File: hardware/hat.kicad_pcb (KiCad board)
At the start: 4 copper layers, 65 x 56.6 mm, 133 parts, among them J101 Raspberry_Pi_2_3, J102 Boot, J201 USB-C, P101 Debug, P201 Black, P301 CON-SENSOR2, P302 CON-SENSOR2, P303 CON-SENSOR2, P304 CON-SENSOR2, P305 CON-SENSOR2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

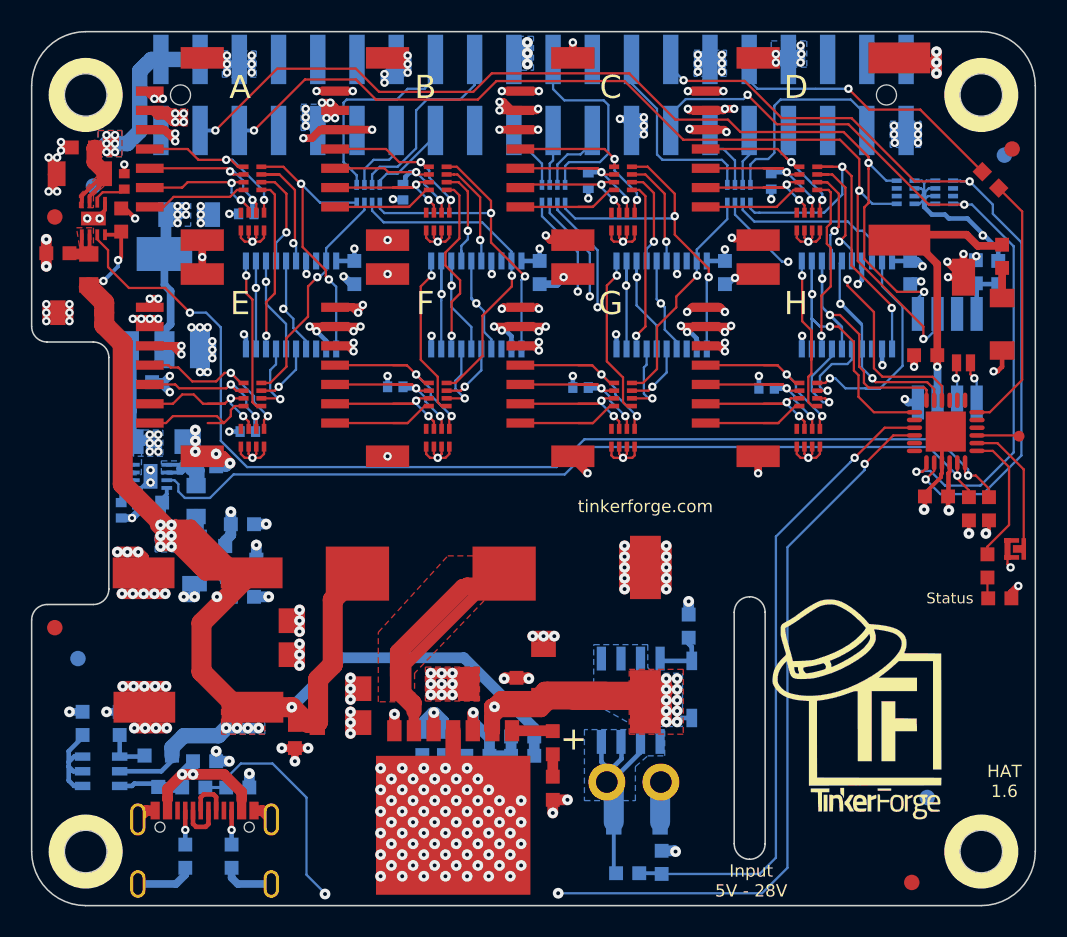
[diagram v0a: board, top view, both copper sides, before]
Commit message: add version 1.7
add step down filters
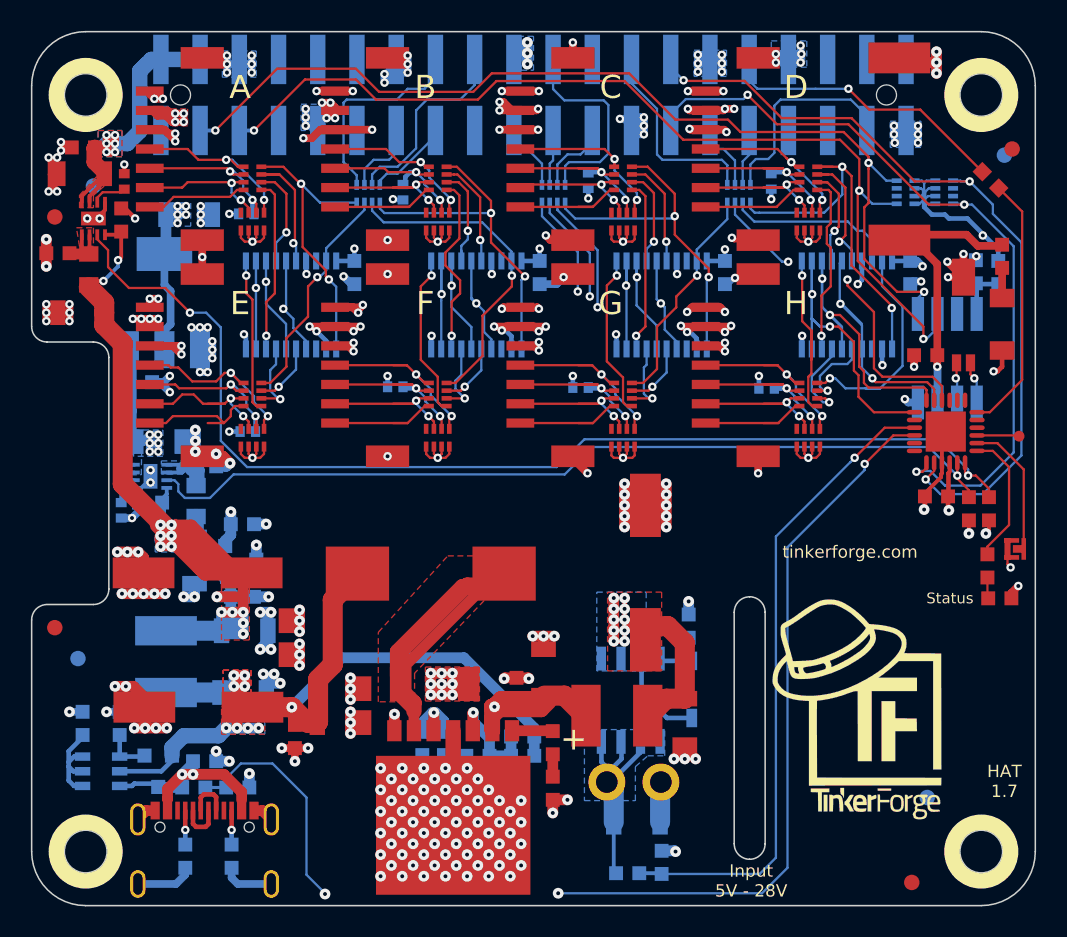
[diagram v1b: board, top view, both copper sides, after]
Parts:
- added C214: 10uF, C1206, F.Cu at (208.5, 70.1)
- added C215: 10uF, C1206, B.Cu at (180.0, 64.2)
- added C216: 10uF, C1206, B.Cu at (179.9, 68.2)
- added L202: 2.2uH 0530CDMCCDS-2R2MC, kicad-libraries:NRS5030, F.Cu at (204.1, 69.7)
- added L203: 2.2uH 0530CDMCCDS-2R2MC, kicad-libraries:NRS5030, B.Cu at (174.9, 66.2)
- moved C202 4.02 mm to (205.9, 60.4)
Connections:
- C202 pad 1: VIN2 -> VIN1
- C206 pad 1: +5V -> 5VF
- C208 pad 1: +5V -> 5VF
- C209 pad 1: +5V -> 5VF
- C210 pad 1: +5V -> 5VF
- C211 pad 1: +5V -> 5VF
- C212 pad 1: +5V -> 5VF
- C213 pad 1: +5V -> 5VF
- D202 pad 2: VIN2 -> VIN1
- L201 pad 2: +5V -> 5VF
- Q201 pad S: +5V -> 5VF
- Q202 pad S: VIN2 -> VIN1
- R209 pad 2: +5V -> 5VF
- U202 pad 5: +5V -> 5VF
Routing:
- net 5VF: track 0.00 -> 61.4 mm, vias 0 -> 9
- net +5V: track 115.9 -> 70.9 mm
- net VIN2: track 54.9 -> 22.8 mm, vias 12 -> 2
- net VIN1: track 0.00 -> 22.4 mm, vias 0 -> 10
- net GND: track 609.9 -> 620.6 mm, vias 290 -> 297
- added copper zone on B.Cu, net 5VF
- added copper zone on F.Cu, net 5VF
- added copper zone on B.Cu, net VIN1
- added copper zone on F.Cu, net VIN1
- removed copper zone on B.Cu, net VIN2
- removed copper zone on F.Cu, net VIN2
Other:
- board text added: "Copyright Tinkerforge GmbH 2021. This documentation describes Open Hardware and is licensed under the CERN OHL v. 1.1. You may redistribute and modify this documentation under the terms of the CERN OHL v.1.1. (http://ohwr.org/cernohl). This documentation is distributed WITHOUT ANY EXPRESS OR IMPLIED WARRANTY, INCLUDING OF MERCHANTABILITY, SATISFACTORY QUALITY AND FITNESS FOR A PARTICULAR PURPOSE.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"
- board text added: "HAT 1.7"
- board text removed: "Copyright Tinkerforge GmbH 2020. This documentation describes Open Hardware and is licensed under the CERN OHL v. 1.1. You may redistribute and modify this documentation under the terms of the CERN OHL v.1.1. (http://ohwr.org/cernohl). This documentation is distributed WITHOUT ANY EXPRESS OR IMPLIED WARRANTY, INCLUDING OF MERCHANTABILITY, SATISFACTORY QUALITY AND FITNESS FOR A PARTICULAR PURPOSE.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"
- board text removed: "HAT 1.6"

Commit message: switched to kicad 6
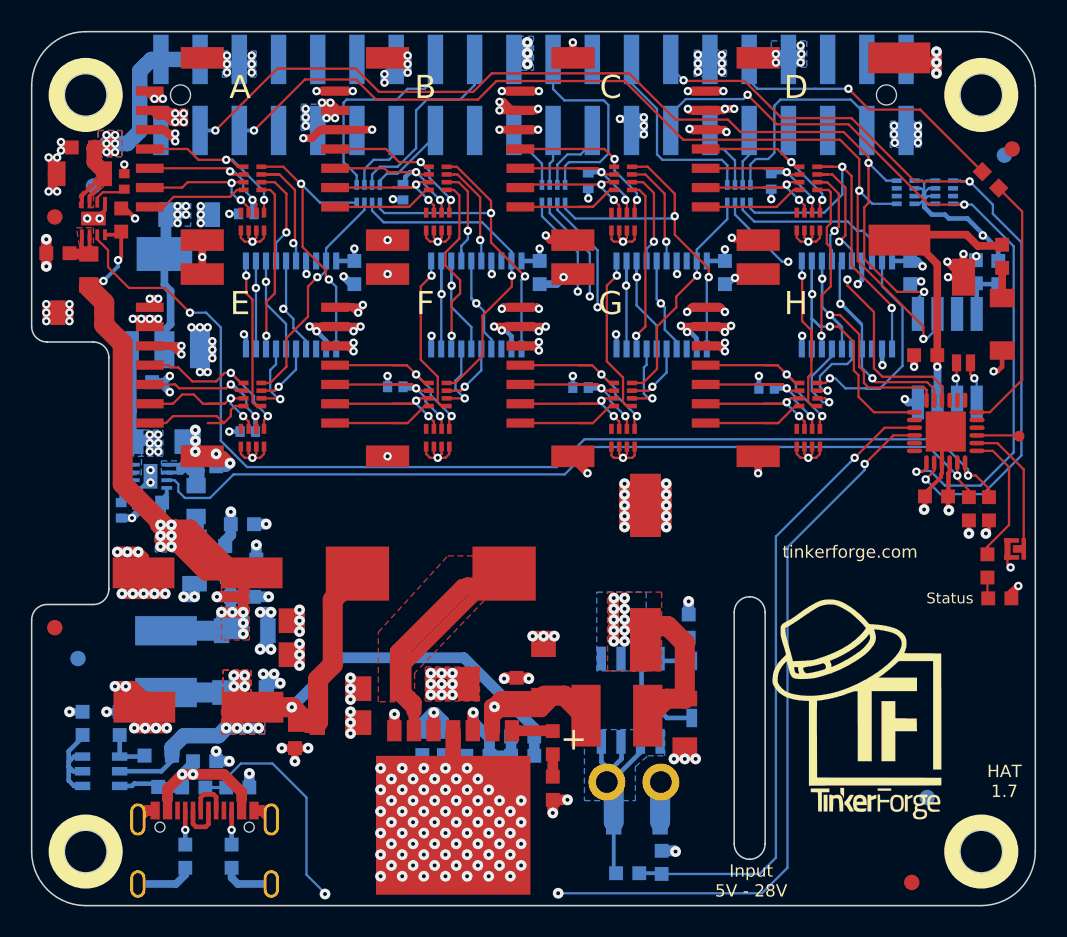
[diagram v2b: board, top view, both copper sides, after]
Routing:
- added copper zone on In2.Cu, net 3V3
- added copper zone on In2.Cu, net B-3V3
- added copper zone on In2.Cu, net B-5V
- added copper zone on In1.Cu, net GND
- removed copper zone on VCC, net 3V3
- removed copper zone on VCC, net B-3V3
- removed copper zone on VCC, net B-5V
- removed copper zone on GND, net GND
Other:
- net class Default removed

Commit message: Proto V1.8
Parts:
- removed C202: UWT1H221MNL1GS, kicad-libraries:ELKO_103
- removed C204, C208: 100nF, C0603F
- removed C205: 100pF, C0603F
- removed C206, C209, C212, C213, C215, C216: 10uF, C1206
- removed C207: 4.7nF, C0603F
- removed C210: 470µF/16V, kicad-libraries:ELKO_83
- removed C211: DNP, C0603F
- removed D201: PMEG6045, SOD-128
- removed Fiducial_Mark (x8): VAL**, kicad-libraries:Fiducial_Mark
- removed the G*** at (198.7, 54.0)
- removed L203: 2.2uH 0530CDMCCDS-2R2MC, kicad-libraries:NRS5030
- removed R201: 27k, R0603F
- removed R206: 20k, R0603F
- removed R209: 47k, R0603F
- removed R210: 8.2k, R0603F
- removed U201: BD906XX-C-HRP7, BD906XX-C-HRP7
- removed VAL: WEEE_7mm, kicad-libraries:WEEE_7mm
- removed VAL: CE_5mm, kicad-libraries:CE_5mm
- added C1: 47uF, kicad-libraries:C1210, F.Cu at (194.2, 67.9)
- added C2: 47uF, kicad-libraries:C1210, F.Cu at (189.8, 67.9)
- added C3: 10uF, kicad-libraries:C0805E, B.Cu at (178.6, 66.9)
- added C4: 10uF, kicad-libraries:C0805E, B.Cu at (176.7, 66.9)
- added C5: 100nF, kicad-libraries:C0603F, B.Cu at (175.1, 66.9)
- added C6: 10uF/50V, kicad-libraries:C1210, F.Cu at (189.8, 59.1)
- added R1: 10k, kicad-libraries:R0603F, F.Cu at (222.2, 55.9)
- added R2: 10k, kicad-libraries:R0603F, F.Cu at (197.0, 65.5)
- added R3: 2k4, kicad-libraries:R0603F, F.Cu at (195.7, 63.9)
- added U1: RPX-4.0, kicad-libraries:RPX-4.0, F.Cu at (192.0, 63.5)
- C203: value 10uF -> 10uF/50V; footprint C1206 -> kicad-libraries:C1210
- C214: value 10uF -> 10uF/50V; footprint C1206 -> kicad-libraries:C1210; moved to B.Cu
- L201: value 22uH 74437368220 -> 2.2uH 0530CDMCCDS-2R2MC; footprint WE-LHMI -> kicad-libraries:NRS5030; moved to B.Cu
- L202: moved to B.Cu
- moved C214 13.1 mm to (206.0, 57.2), turned to 0 degrees
- moved L202 13.0 mm to (200.4, 57.2)
- moved L201 10.8 mm to (183.3, 66.9)
- moved C203 9.35 mm to (194.2, 59.1), turned to 180 degrees
- moved G*** 0.46 mm to (220.1, 69.4)
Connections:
- CP301 pad 4: Net-(CP301-Pad4) -> unconnected-(CP301-Pad4)
- CP302 pad 4: Net-(CP302-Pad4) -> unconnected-(CP302-Pad4)
- CP303 pad 4: Net-(CP303-Pad4) -> unconnected-(CP303-Pad4)
- CP304 pad 4: Net-(CP304-Pad4) -> unconnected-(CP304-Pad4)
- CP305 pad 4: Net-(CP305-Pad4) -> unconnected-(CP305-Pad4)
- CP306 pad 4: Net-(CP306-Pad4) -> unconnected-(CP306-Pad4)
- CP307 pad 4: Net-(CP307-Pad4) -> unconnected-(CP307-Pad4)
- CP308 pad 4: Net-(CP308-Pad4) -> unconnected-(CP308-Pad4)
- J101 pad 1: Net-(J101-Pad1) -> unconnected-(J101-Pad1)
- J101 pad 10: Net-(J101-Pad10) -> unconnected-(J101-Pad10)
- J101 pad 11: Net-(J101-Pad11) -> unconnected-(J101-Pad11)
- J101 pad 12: Net-(J101-Pad12) -> unconnected-(J101-Pad12)
- J101 pad 17: Net-(J101-Pad17) -> unconnected-(J101-Pad17)
- J101 pad 24: Net-(J101-Pad24) -> unconnected-(J101-Pad24)
- J101 pad 33: Net-(J101-Pad33) -> unconnected-(J101-Pad33)
- J101 pad 35: Net-(J101-Pad35) -> unconnected-(J101-Pad35)
- J101 pad 36: Net-(J101-Pad36) -> unconnected-(J101-Pad36)
- J101 pad 38: Net-(J101-Pad38) -> unconnected-(J101-Pad38)
- J101 pad 40: Net-(J101-Pad40) -> unconnected-(J101-Pad40)
- J101 pad 7: Net-(J101-Pad7) -> unconnected-(J101-Pad7)
- J101 pad 8: Net-(J101-Pad8) -> unconnected-(J101-Pad8)
- J201 pad 2: Net-(J201-Pad2) -> unconnected-(J201-Pad2)
- J201 pad 3: Net-(J201-Pad3) -> unconnected-(J201-Pad3)
- L201 pad 2: 5VF -> +5V
- Q201 pad S: 5VF -> VSW
- RP101 pad 6: Net-(RP101-Pad6) -> unconnected-(RP101-Pad6)
- RP101 pad 7: Net-(RP101-Pad7) -> unconnected-(RP101-Pad7)
- RP105 pad 6: Net-(RP105-Pad6) -> unconnected-(RP105-Pad6)
- RP105 pad 7: Net-(RP105-Pad7) -> unconnected-(RP105-Pad7)
- U101 pad 16: Net-(U101-Pad16) -> GND
- U101 pad 17: Net-(U101-Pad17) -> unconnected-(U101-Pad17)
- U101 pad 19: Net-(U101-Pad19) -> unconnected-(U101-Pad19)
- U101 pad 2: Net-(U101-Pad2) -> unconnected-(U101-Pad2)
- U101 pad 20: Net-(U101-Pad20) -> unconnected-(U101-Pad20)
- U101 pad 21: Net-(U101-Pad21) -> unconnected-(U101-Pad21)
- U101 pad 5: Net-(U101-Pad5) -> unconnected-(U101-Pad5)
- U101 pad 6: Net-(U101-Pad6) -> PowerGood
- U105 pad 7: Net-(U105-Pad7) -> unconnected-(U105-Pad7)
- U202 pad 5: 5VF -> VSW
- U301 pad 18: Net-(U301-Pad18) -> unconnected-(U301-Pad18)
- U301 pad 3: Net-(U301-Pad3) -> unconnected-(U301-Pad3)
- U302 pad 18: Net-(U302-Pad18) -> unconnected-(U302-Pad18)
- U302 pad 3: Net-(U302-Pad3) -> unconnected-(U302-Pad3)
- U303 pad 18: Net-(U303-Pad18) -> unconnected-(U303-Pad18)
- U303 pad 3: Net-(U303-Pad3) -> unconnected-(U303-Pad3)
- U304 pad 18: Net-(U304-Pad18) -> unconnected-(U304-Pad18)
- U304 pad 3: Net-(U304-Pad3) -> unconnected-(U304-Pad3)
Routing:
- net GND: track 620.6 -> 227.1 mm, vias 297 -> 275
- net 5VF: track 61.4 -> 0.00 mm, vias 9 -> 0
- net PowerGood: track 0.00 -> 57.7 mm, vias 0 -> 2
- net B-3V3: track 102.5 -> 50.4 mm
- net VIN2: track 22.8 -> 1.27 mm, vias 2 -> 8
- net VIN1: track 22.4 -> 5.62 mm, vias 10 -> 0
- net +5V: track 70.9 -> 55.3 mm, vias 14 -> 20
- net VSW: track 34.6 -> 20.6 mm, vias 0 -> 8
- net Net-(C211-Pad2): track 7.07 -> 0.00 mm, vias 1 -> 0
- net Net-(C205-Pad1): track 4.38 -> 0.00 mm, vias 1 -> 0
- net unconnected-(J201-Pad2): track 0.00 -> 2.88 mm
- net Net-(J201-Pad2): track 2.88 -> 0.00 mm
- net unconnected-(J201-Pad3): track 0.00 -> 2.88 mm
- net Net-(J201-Pad3): track 2.88 -> 0.00 mm
- net Net-(R2-Pad2): track 0.00 -> 2.79 mm
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- added copper zone on B.Cu, net VIN2
- added copper zone on F.Cu, net VIN2
- added copper zone on B.Cu, net VSW
- removed copper zone on B.Cu, net 5VF
- removed copper zone on F.Cu, net 5VF
- removed copper zone on F.Cu, net VIN1
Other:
- board text added: "-"
- board text added: "HAT 1.8"
- board text added: "Input 5V - 36V"
- board text removed: "HAT 1.7"
- board text removed: "Input 5V - 28V"

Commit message: ready for prototype
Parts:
- moved R205 1.98 mm to (208.4, 77.8)
- moved C214 1.10 mm to (206.0, 58.3)
- moved L202 1.10 mm to (200.4, 58.3)
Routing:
- net +5V: track 55.3 -> 35.0 mm
- net GND: track 227.1 -> 231.6 mm, vias 275 -> 297
- net DC-IN-VOLTAGE: track 42.1 -> 45.8 mm

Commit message: changed D101
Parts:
- D101: value BAQ33-GS08 -> FDLL3595
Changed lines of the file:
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@@
       (drillshape 0)
       (scaleselection 1)
-      (outputdirectory "pcb/")
+      (outputdirectory "HAT_1V8_Gerber/")
     )
   )
@@
       (effects (font (size 0.29972 0.29972) (thickness 0.07493)))
     )
-    (fp_text value "BAQ33-GS08" (at 0.23 -0.24 90) (layer "F.Fab")
+    (fp_text value "FDLL3595" (at 0.23 -0.24 90) (layer "F.Fab")
       (effects (font (size 0.29972 0.29972) (thickness 0.07493)))
     )

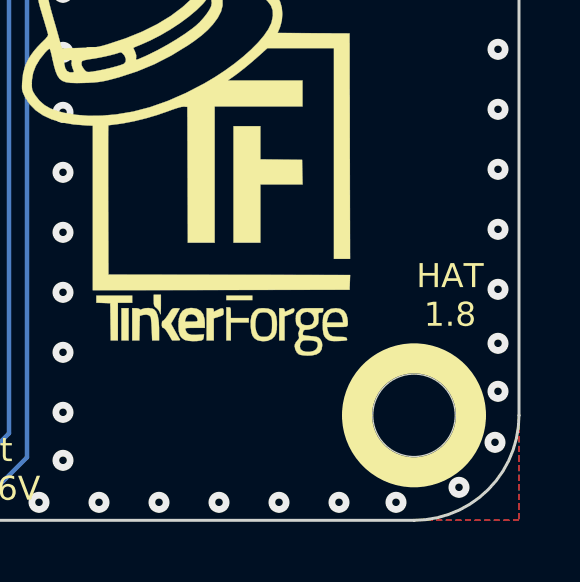
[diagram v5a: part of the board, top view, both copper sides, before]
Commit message: Hardware V1.9 changed zone infill on the + side of OQ2
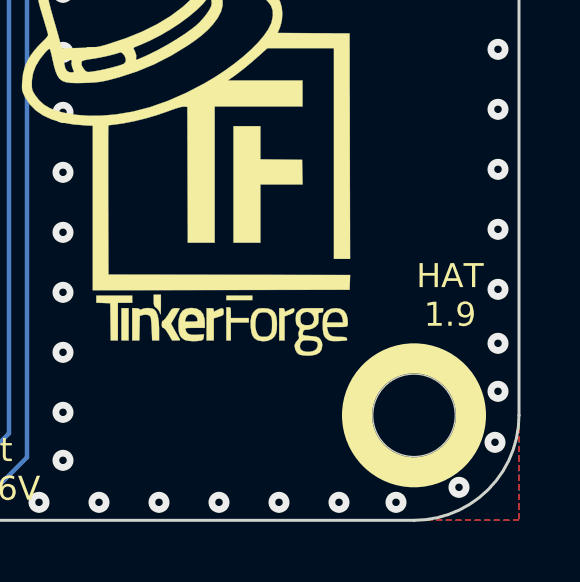
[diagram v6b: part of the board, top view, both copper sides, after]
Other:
- board text added: "HAT 1.9"
- board text removed: "HAT 1.8"
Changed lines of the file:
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@@
   (title_block
     (title "HAT Bricklet")
-    (date "2023-05-15")
-    (rev "1.8")
+    (date "2023-06-29")
+    (rev "1.9")
     (company "Tinkerforge GmbH")
     (comment 1 "Licensed under CERN OHL v.1.1")
@@
     (effects (font (size 1.5 1.5) (thickness 0.3)))
   )
-  (gr_text "HAT\n1.8" (at 228.9 74.5) (layer "F.SilkS")
+  (gr_text "HAT\n1.9" (at 228.9 74.5) (layer "F.SilkS")
     (effects (font (size 0.8 0.8) (thickness 0.15)))
   )
@@
         (xy 208.9 77.9)
         (xy 201.5 77.9)
-        (xy 201.5 72.2)
-        (xy 208.9 72.2)
+        (xy 201.5 75.2)
+        (xy 205.3 75.2)
+        (xy 205.3 73)
+        (xy 206.1 72.3)
+        (xy 208.9 72.3)
       )
     )

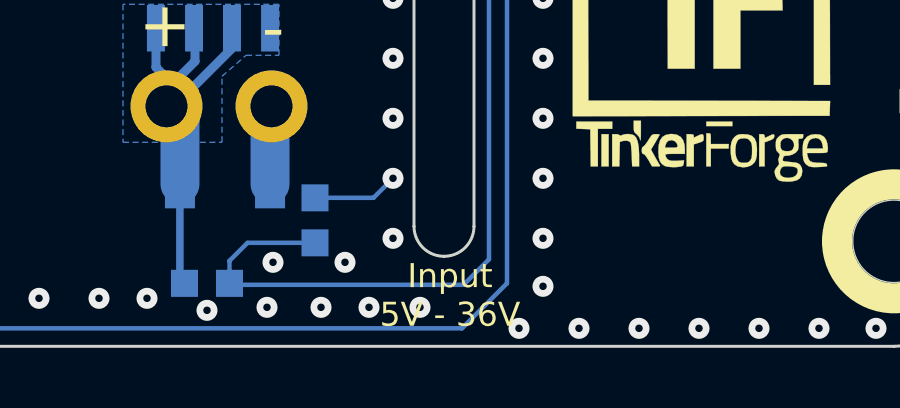
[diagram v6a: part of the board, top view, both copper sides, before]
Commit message: hardware: changed input silkscreen to 6V-36V
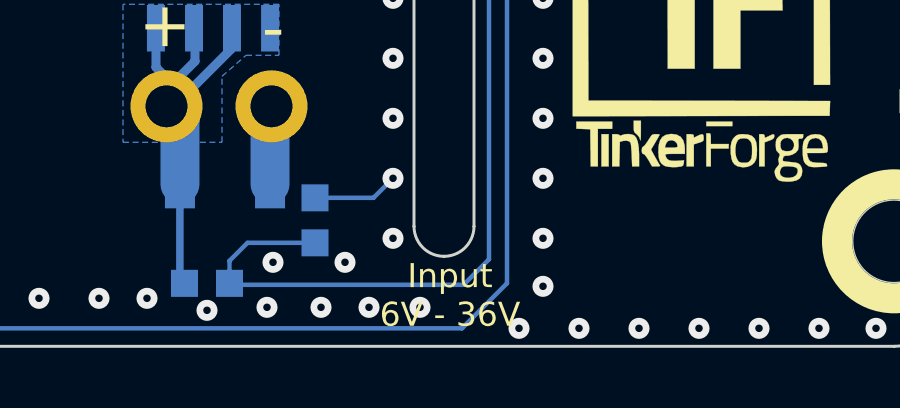
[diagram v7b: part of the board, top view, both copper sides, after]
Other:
- board text added: "Input 6V - 36V"
- board text removed: "Input 5V - 36V"
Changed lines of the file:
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@@
     (effects (font (size 1.5 1.524) (thickness 0.3)))
   )
-  (gr_text "Input\n5V - 36V" (at 212.9 80.3) (layer "F.SilkS")
+  (gr_text "Input\n6V - 36V" (at 212.9 80.3) (layer "F.SilkS")
     (effects (font (size 0.8 0.8) (thickness 0.15)))
   )

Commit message: move to kicad 7
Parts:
- D202: footprint SOD-123 -> kicad-libraries:SOD-123
- Q201: footprint SOT23GDS -> kicad-libraries:SOT23GDS
- R218: footprint R1206 -> kicad-libraries:R1206
- U101: footprint QFN24-4x4mm-0.5mm -> kicad-libraries:QFN24-4x4mm-0.5mm
- U103, U104: footprint WSON8-2x2 -> kicad-libraries:WSON8-2x2
- U202: footprint SOT26 -> kicad-libraries:SOT26
